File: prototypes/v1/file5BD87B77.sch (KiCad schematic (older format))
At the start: 5 parts, among them U1 74LS10, U3 74LS04, U4 74LS20, U6 74LS00, U7 74LS04

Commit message: finish logic
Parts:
- renumbered U6 to U10, U7 to U13, U3 to U2, U1 to U4, U4 to U8
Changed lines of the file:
@@
 AR Path="/5BD91A8E/5BD8F209" Ref="U?"  Part="7"
 AR Path="/5BD8F209" Ref="U?"  Part="7"
-AR Path="/5BD87B78/5BD8F209" Ref="U3"  Part="7"
-F 0 "U3" H 2180 1396 50  0000 L CNN
+AR Path="/5BD87B78/5BD8F209" Ref="U2"  Part="7"
+F 0 "U2" H 2180 1396 50  0000 L CNN
 F 1 "74LS04" H 2180 1305 50  0000 L CNN
 F 2 "" H 1950 1350 50  0001 C CNN
@@
 AR Path="/5BD91A8E/5BD8F210" Ref="U?"  Part="5"
 AR Path="/5BD8F210" Ref="U?"  Part="5"
-AR Path="/5BD87B78/5BD8F210" Ref="U6"  Part="5"
-F 0 "U6" H 2980 1396 50  0000 L CNN
+AR Path="/5BD87B78/5BD8F210" Ref="U10"  Part="5"
+F 0 "U10" H 2980 1396 50  0000 L CNN
 F 1 "74LS00" H 2980 1305 50  0000 L CNN
 F 2 "" H 2750 1350 50  0001 C CNN
@@
 AR Path="/5BD91A8E/5BD8F217" Ref="U?"  Part="7"
 AR Path="/5BD8F217" Ref="U?"  Part="7"
-AR Path="/5BD87B78/5BD8F217" Ref="U7"  Part="7"
-F 0 "U7" H 3830 1396 50  0000 L CNN
+AR Path="/5BD87B78/5BD8F217" Ref="U13"  Part="7"
+F 0 "U13" H 3830 1396 50  0000 L CNN
 F 1 "74LS04" H 3830 1305 50  0000 L CNN
 F 2 "" H 3600 1350 50  0001 C CNN
@@
 AR Path="/5BD91A8E/5BD8F224" Ref="#PWR?"  Part="1"
 AR Path="/5BD8F224" Ref="#PWR?"  Part="1"
-AR Path="/5BD87B78/5BD8F224" Ref="#PWR05"  Part="1"
-F 0 "#PWR05" H 3750 1700 50  0001 C CNN
+AR Path="/5BD87B78/5BD8F224" Ref="#PWR022"  Part="1"
+F 0 "#PWR022" H 3750 1700 50  0001 C CNN
 F 1 "GND" H 3755 1777 50  0000 C CNN
 F 2 "" H 3750 1950 50  0001 C CNN
@@
 AR Path="/5BD91A8E/5BD8F22A" Ref="#PWR?"  Part="1"
 AR Path="/5BD8F22A" Ref="#PWR?"  Part="1"
-AR Path="/5BD87B78/5BD8F22A" Ref="#PWR04"  Part="1"
-F 0 "#PWR04" H 2900 1700 50  0001 C CNN
+AR Path="/5BD87B78/5BD8F22A" Ref="#PWR021"  Part="1"
+F 0 "#PWR021" H 2900 1700 50  0001 C CNN
 F 1 "GND" H 2905 1777 50  0000 C CNN
 F 2 "" H 2900 1950 50  0001 C CNN
@@
 AR Path="/5BD91A8E/5BD8F230" Ref="#PWR?"  Part="1"
 AR Path="/5BD8F230" Ref="#PWR?"  Part="1"
-AR Path="/5BD87B78/5BD8F230" Ref="#PWR03"  Part="1"
-F 0 "#PWR03" H 2100 1700 50  0001 C CNN
+AR Path="/5BD87B78/5BD8F230" Ref="#PWR020"  Part="1"
+F 0 "#PWR020" H 2100 1700 50  0001 C CNN
 F 1 "GND" H 2105 1777 50  0000 C CNN
 F 2 "" H 2100 1950 50  0001 C CNN
@@
 AR Path="/5BD91A8E/5BD8F23C" Ref="U?"  Part="3"
 AR Path="/5BD8F23C" Ref="U?"  Part="3"
-AR Path="/5BD87B78/5BD8F23C" Ref="U4"  Part="3"
-F 0 "U4" H 1330 1446 50  0000 L CNN
+AR Path="/5BD87B78/5BD8F23C" Ref="U8"  Part="3"
+F 0 "U8" H 1330 1446 50  0000 L CNN
 F 1 "74LS20" H 1330 1355 50  0000 L CNN
 F 2 "" H 1100 1400 50  0001 C CNN
@@
 AR Path="/5BD91A8E/5BD8F244" Ref="#PWR?"  Part="1"
 AR Path="/5BD8F244" Ref="#PWR?"  Part="1"
-AR Path="/5BD87B78/5BD8F244" Ref="#PWR01"  Part="1"
-F 0 "#PWR01" H 1250 1700 50  0001 C CNN
+AR Path="/5BD87B78/5BD8F244" Ref="#PWR018"  Part="1"
+F 0 "#PWR018" H 1250 1700 50  0001 C CNN
 F 1 "GND" H 1255 1777 50  0000 C CNN
 F 2 "" H 1250 1950 50  0001 C CNN
@@
 P 4450 1350
 AR Path="/5BDA73F4" Ref="U?"  Part="4"
-AR Path="/5BD87B78/5BDA73F4" Ref="U1"  Part="4"
-F 0 "U1" H 4680 1396 50  0000 L CNN
+AR Path="/5BD87B78/5BDA73F4" Ref="U4"  Part="4"
+F 0 "U4" H 4680 1396 50  0000 L CNN
 F 1 "74LS10" H 4680 1305 50  0000 L CNN
 F 2 "" H 4450 1350 50  0001 C CNN
@@
 P 4600 1850
 AR Path="/5BDA73FC" Ref="#PWR?"  Part="1"
-AR Path="/5BD87B78/5BDA73FC" Ref="#PWR06"  Part="1"
-F 0 "#PWR06" H 4600 1600 50  0001 C CNN
+AR Path="/5BD87B78/5BDA73FC" Ref="#PWR023"  Part="1"
+F 0 "#PWR023" H 4600 1600 50  0001 C CNN
 F 1 "GND" H 4605 1677 50  0000 C CNN
 F 2 "" H 4600 1850 50  0001 C CNN
@@
 	1750 3150 1900 3150
 $Comp
-L power:+5V #PWR02
+L power:+5V #PWR019
 U 1 1 5BDEC84E
 P 1900 2950
-F 0 "#PWR02" H 1900 2800 50  0001 C CNN
+F 0 "#PWR019" H 1900 2800 50  0001 C CNN
 F 1 "+5V" H 1915 3123 50  0000 C CNN
 F 2 "" H 1900 2950 50  0001 C CNN

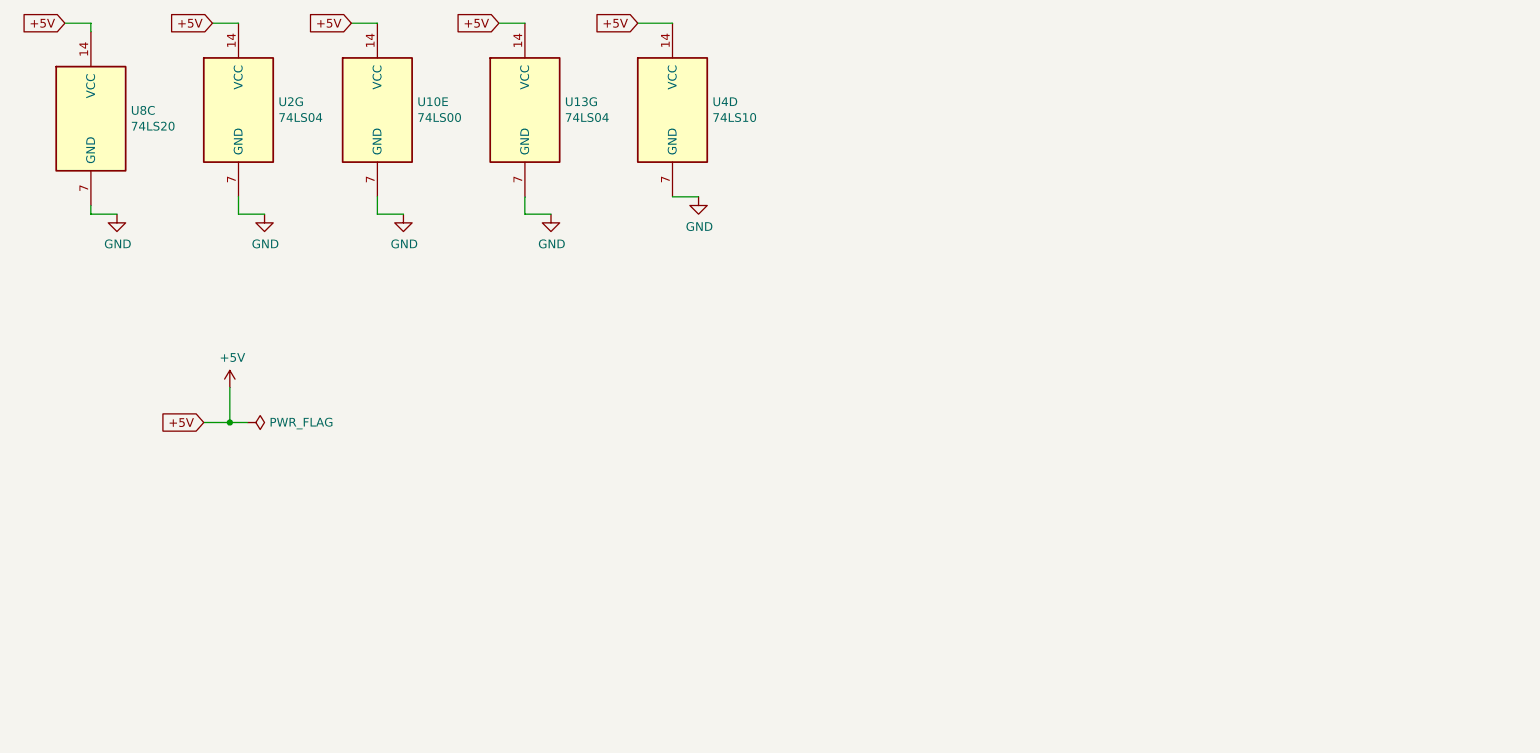
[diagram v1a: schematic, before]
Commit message: optimized logic
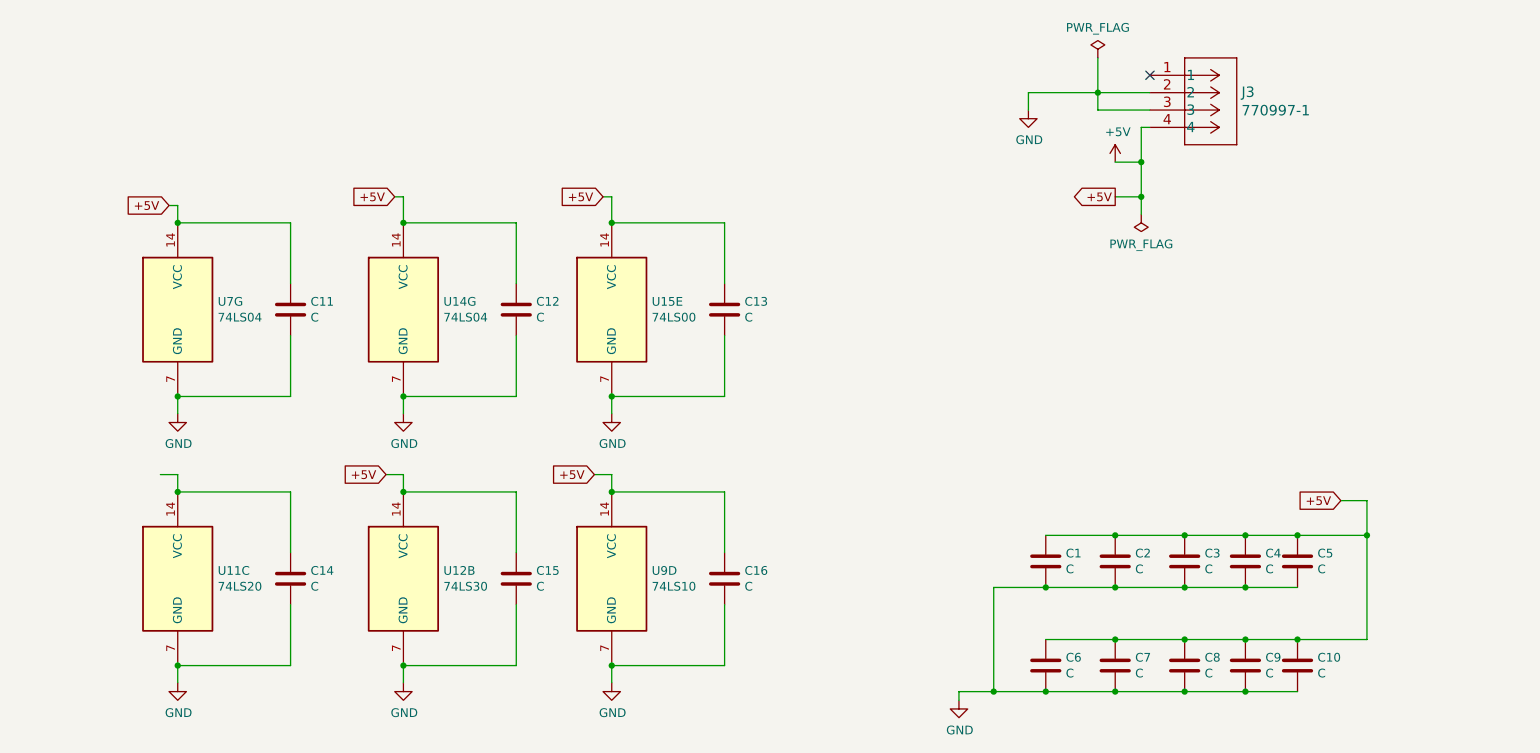
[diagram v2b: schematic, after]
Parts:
- removed U10: 74LS00, symbol 74xx:74LS00
- removed U13, U2: 74LS04, symbol 74xx:74LS04
- removed U4: 74LS10, symbol 74xx:74LS10
- removed U8: 74LS20, symbol 74xx:74LS20
- added C1: C, Capacitors_ThroughHole:C_Disc_D6.0mm_W4.4mm_P5.00mm, symbol Device:C
- added C10, C11, C12, C13, C14, C15, C16, C2, C3, C4, C5, C6, C7, C8, C9: C, symbol Device:C
- added J3: 770997-1, footprints:770997-1, symbol symbols:770997-1
- added U11: 74LS20, symbol 74xx:74LS20
- added U12: 74LS30, symbol 74xx:74LS30
- added U14, U7: 74LS04, symbol 74xx:74LS04
- added U15: 74LS00, symbol 74xx:74LS00
- added U9: 74LS10, symbol 74xx:74LS10
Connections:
- net +5V: now also C1.1, C10.1, C11.1, C12.1, C13.1, C15.1, C16.1, C2.1, C3.1, C4.1, C5.1, C6.1, C7.1, C8.1, C9.1, J3.4, U12.14 (VCC), U14.14 (VCC), U15.14 (VCC), U7.14 (VCC), U9.14 (VCC)
- net GND: now also C1.2, C10.2, C11.2, C12.2, C13.2, C14.2, C15.2, C16.2, C2.2, C3.2, C4.2, C5.2, C6.2, C7.2, C8.2, C9.2, J3.2, J3.3, U11.7 (GND), U12.7 (GND), U14.7 (GND), U15.7 (GND), U7.7 (GND), U9.7 (GND)
- new net: C14.1, U11.14 (VCC)
- no-connect marks 0 -> 1

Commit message: gerbers created, Rev 0 sent to manufacturer
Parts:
- added C17, C18, C19, C20: C, Capacitors_ThroughHole:C_Disc_D6.0mm_W4.4mm_P5.00mm, symbol Device:C
- C10, C11, C12, C13, C14, C15, C16, C2, C3, C4, C5, C6, C7, C8, C9: footprint (none) -> Capacitors_ThroughHole:C_Disc_D6.0mm_W4.4mm_P5.00mm
- U11, U12, U14, U15, U7, U9: footprint (none) -> Package_DIP:DIP-14_W7.62mm
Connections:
- net +5V: now also C14.1, U11.14 (VCC), C17.1, C18.1, C19.1, C20.1
- net GND: now also C17.2, C18.2, C19.2, C20.2
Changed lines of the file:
@@
 F 0 "C2" H 7115 3996 50  0000 L CNN
 F 1 "C" H 7115 3905 50  0000 L CNN
-F 2 "" H 7038 3800 50  0001 C CNN
+F 2 "Capacitors_ThroughHole:C_Disc_D6.0mm_W4.4mm_P5.00mm" H 7038 3800 50  0001 C CNN
 F 3 "~" H 7000 3950 50  0001 C CNN
 	1    7000 3950
@@
 F 0 "C3" H 7515 3996 50  0000 L CNN
 F 1 "C" H 7515 3905 50  0000 L CNN
-F 2 "" H 7438 3800 50  0001 C CNN
+F 2 "Capacitors_ThroughHole:C_Disc_D6.0mm_W4.4mm_P5.00mm" H 7438 3800 50  0001 C CNN
 F 3 "~" H 7400 3950 50  0001 C CNN
 	1    7400 3950
@@
 F 0 "C4" H 7865 3996 50  0000 L CNN
 F 1 "C" H 7865 3905 50  0000 L CNN
-F 2 "" H 7788 3800 50  0001 C CNN
+F 2 "Capacitors_ThroughHole:C_Disc_D6.0mm_W4.4mm_P5.00mm" H 7788 3800 50  0001 C CNN
 F 3 "~" H 7750 3950 50  0001 C CNN
 	1    7750 3950
@@
 F 0 "C5" H 8165 3996 50  0000 L CNN
 F 1 "C" H 8165 3905 50  0000 L CNN
-F 2 "" H 8088 3800 50  0001 C CNN
+F 2 "Capacitors_ThroughHole:C_Disc_D6.0mm_W4.4mm_P5.00mm" H 8088 3800 50  0001 C CNN
 F 3 "~" H 8050 3950 50  0001 C CNN
 	1    8050 3950
@@
 F 0 "C6" H 6715 4596 50  0000 L CNN
 F 1 "C" H 6715 4505 50  0000 L CNN
-F 2 "" H 6638 4400 50  0001 C CNN
+F 2 "Capacitors_ThroughHole:C_Disc_D6.0mm_W4.4mm_P5.00mm" H 6638 4400 50  0001 C CNN
 F 3 "~" H 6600 4550 50  0001 C CNN
 	1    6600 4550
@@
 F 0 "C7" H 7115 4596 50  0000 L CNN
 F 1 "C" H 7115 4505 50  0000 L CNN
-F 2 "" H 7038 4400 50  0001 C CNN
+F 2 "Capacitors_ThroughHole:C_Disc_D6.0mm_W4.4mm_P5.00mm" H 7038 4400 50  0001 C CNN
 F 3 "~" H 7000 4550 50  0001 C CNN
 	1    7000 4550
@@
 F 0 "C8" H 7515 4596 50  0000 L CNN
 F 1 "C" H 7515 4505 50  0000 L CNN
-F 2 "" H 7438 4400 50  0001 C CNN
+F 2 "Capacitors_ThroughHole:C_Disc_D6.0mm_W4.4mm_P5.00mm" H 7438 4400 50  0001 C CNN
 F 3 "~" H 7400 4550 50  0001 C CNN
 	1    7400 4550
@@
 F 0 "C9" H 7865 4596 50  0000 L CNN
 F 1 "C" H 7865 4505 50  0000 L CNN
-F 2 "" H 7788 4400 50  0001 C CNN
+F 2 "Capacitors_ThroughHole:C_Disc_D6.0mm_W4.4mm_P5.00mm" H 7788 4400 50  0001 C CNN
 F 3 "~" H 7750 4550 50  0001 C CNN
 	1    7750 4550
@@
 F 0 "C10" H 8165 4596 50  0000 L CNN
 F 1 "C" H 8165 4505 50  0000 L CNN
-F 2 "" H 8088 4400 50  0001 C CNN
+F 2 "Capacitors_ThroughHole:C_Disc_D6.0mm_W4.4mm_P5.00mm" H 8088 4400 50  0001 C CNN
 F 3 "~" H 8050 4550 50  0001 C CNN
 	1    8050 4550
@@
 Wire Wire Line
 	7750 4400 8050 4400
-Text GLabel 8300 3600 0    50   Input ~ 0
+Text GLabel 9200 3600 0    50   Input ~ 0
 +5V
 $Comp
@@
 F 0 "U7" H 1830 2546 50  0000 L CNN
 F 1 "74LS04" H 1830 2455 50  0000 L CNN
-F 2 "" H 1600 2500 50  0001 C CNN
+F 2 "Package_DIP:DIP-14_W7.62mm" H 1600 2500 50  0001 C CNN
 F 3 "http://www.ti.com/lit/gpn/sn74LS04" H 1600 2500 50  0001 C CNN
 	7    1600 2500
@@
 F 0 "U14" H 3130 2546 50  0000 L CNN
 F 1 "74LS04" H 3130 2455 50  0000 L CNN
-F 2 "" H 2900 2500 50  0001 C CNN
+F 2 "Package_DIP:DIP-14_W7.62mm" H 2900 2500 50  0001 C CNN
 F 3 "http://www.ti.com/lit/gpn/sn74LS04" H 2900 2500 50  0001 C CNN
 	7    2900 2500
@@
 F 0 "U15" H 4330 2546 50  0000 L CNN
 F 1 "74LS00" H 4330 2455 50  0000 L CNN
-F 2 "" H 4100 2500 50  0001 C CNN
+F 2 "Package_DIP:DIP-14_W7.62mm" H 4100 2500 50  0001 C CNN
 F 3 "http://www.ti.com/lit/gpn/sn74ls00" H 4100 2500 50  0001 C CNN
 	5    4100 2500
@@
 F 0 "U9" H 4330 4096 50  0000 L CNN
 F 1 "74LS10" H 4330 4005 50  0000 L CNN
-F 2 "" H 4100 4050 50  0001 C CNN
+F 2 "Package_DIP:DIP-14_W7.62mm" H 4100 4050 50  0001 C CNN
 F 3 "http://www.ti.com/lit/gpn/sn74LS10" H 4100 4050 50  0001 C CNN
 	4    4100 4050
@@
 F 0 "U11" H 1830 4096 50  0000 L CNN
 F 1 "74LS20" H 1830 4005 50  0000 L CNN
-F 2 "" H 1600 4050 50  0001 C CNN
+F 2 "Package_DIP:DIP-14_W7.62mm" H 1600 4050 50  0001 C CNN
 F 3 "http://www.ti.com/lit/gpn/sn74LS20" H 1600 4050 50  0001 C CNN
 	3    1600 4050
@@
 F 0 "U12" H 3130 4096 50  0000 L CNN
 F 1 "74LS30" H 3130 4005 50  0000 L CNN
-F 2 "" H 2900 4050 50  0001 C CNN
+F 2 "Package_DIP:DIP-14_W7.62mm" H 2900 4050 50  0001 C CNN
 F 3 "http://www.ti.com/lit/gpn/sn74LS30" H 2900 4050 50  0001 C CNN
 	2    2900 4050
@@
 F 0 "C15" H 3665 4096 50  0000 L CNN
 F 1 "C" H 3665 4005 50  0000 L CNN
-F 2 "" H 3588 3900 50  0001 C CNN
+F 2 "Capacitors_ThroughHole:C_Disc_D6.0mm_W4.4mm_P5.00mm" H 3588 3900 50  0001 C CNN
 F 3 "~" H 3550 4050 50  0001 C CNN
 	1    3550 4050
@@
 F 0 "C14" H 2365 4096 50  0000 L CNN
 F 1 "C" H 2365 4005 50  0000 L CNN
-F 2 "" H 2288 3900 50  0001 C CNN
+F 2 "Capacitors_ThroughHole:C_Disc_D6.0mm_W4.4mm_P5.00mm" H 2288 3900 50  0001 C CNN
 F 3 "~" H 2250 4050 50  0001 C CNN
 	1    2250 4050
@@
 F 0 "C16" H 4865 4096 50  0000 L CNN
 F 1 "C" H 4865 4005 50  0000 L CNN
-F 2 "" H 4788 3900 50  0001 C CNN
+F 2 "Capacitors_ThroughHole:C_Disc_D6.0mm_W4.4mm_P5.00mm" H 4788 3900 50  0001 C CNN
 F 3 "~" H 4750 4050 50  0001 C CNN
 	1    4750 4050
@@
 F 0 "C11" H 2365 2546 50  0000 L CNN
 F 1 "C" H 2365 2455 50  0000 L CNN
-F 2 "" H 2288 2350 50  0001 C CNN
+F 2 "Capacitors_ThroughHole:C_Disc_D6.0mm_W4.4mm_P5.00mm" H 2288 2350 50  0001 C CNN
 F 3 "~" H 2250 2500 50  0001 C CNN
 	1    2250 2500
@@
 F 0 "C12" H 3665 2546 50  0000 L CNN
 F 1 "C" H 3665 2455 50  0000 L CNN
-F 2 "" H 3588 2350 50  0001 C CNN
+F 2 "Capacitors_ThroughHole:C_Disc_D6.0mm_W4.4mm_P5.00mm" H 3588 2350 50  0001 C CNN
 F 3 "~" H 3550 2500 50  0001 C CNN
 	1    3550 2500
@@
 F 0 "C13" H 4865 2546 50  0000 L CNN
 F 1 "C" H 4865 2455 50  0000 L CNN
-F 2 "" H 4788 2350 50  0001 C CNN
+F 2 "Capacitors_ThroughHole:C_Disc_D6.0mm_W4.4mm_P5.00mm" H 4788 2350 50  0001 C CNN
 F 3 "~" H 4750 2500 50  0001 C CNN
 	1    4750 2500
@@
 Connection ~ 1600 3000
 Wire Wire Line
-	8050 3800 8450 3800
-Wire Wire Line
-	8450 3800 8450 4400
-Wire Wire Line
-	8450 4400 8050 4400
+	9350 3800 9350 4400
+Wire Wire Line
+	9200 3600 9350 3600
+Wire Wire Line
+	9350 3600 9350 3800
+Connection ~ 9350 3800
+$Comp
+L Device:C C17
+U 1 1 5BDD839C
+P 8350 3950
+F 0 "C17" H 8465 3996 50  0000 L CNN
+F 1 "C" H 8465 3905 50  0000 L CNN
+F 2 "Capacitors_ThroughHole:C_Disc_D6.0mm_W4.4mm_P5.00mm" H 8388 3800 50  0001 C CNN
+F 3 "~" H 8350 3950 50  0001 C CNN
+	1    8350 3950
+	1    0    0    -1
+$EndComp
+$Comp
+L Device:C C19
+U 1 1 5BDD83FC
+P 8650 3950
+F 0 "C19" H 8765 3996 50  0000 L CNN
+F 1 "C" H 8765 3905 50  0000 L CNN
+F 2 "Capacitors_ThroughHole:C_Disc_D6.0mm_W4.4mm_P5.00mm" H 8688 3800 50  0001 C CNN
+F 3 "~" H 8650 3950 50  0001 C CNN
+	1    8650 3950
+	1    0    0    -1
+$EndComp
+$Comp
+L Device:C C18
+U 1 1 5BDD844C
+P 8350 4550
+F 0 "C18" H 8465 4596 50  0000 L CNN
+F 1 "C" H 8465 4505 50  0000 L CNN
+F 2 "Capacitors_ThroughHole:C_Disc_D6.0mm_W4.4mm_P5.00mm" H 8388 4400 50  0001 C CNN
+F 3 "~" H 8350 4550 50  0001 C CNN
+	1    8350 4550
+	1    0    0    -1
+$EndComp
+$Comp
+L Device:C C20
+U 1 1 5BDD84AE
+P 8650 4550
+F 0 "C20" H 8765 4596 50  0000 L CNN
+F 1 "C" H 8765 4505 50  0000 L CNN
+F 2 "Capacitors_ThroughHole:C_Disc_D6.0mm_W4.4mm_P5.00mm" H 8688 4400 50  0001 C CNN
+F 3 "~" H 8650 4550 50  0001 C CNN
+	1    8650 4550
+	1    0    0    -1
+$EndComp
+Wire Wire Line
+	8050 3800 8350 3800
 Connection ~ 8050 3800
+Connection ~ 8350 3800
+Wire Wire Line
+	8350 3800 8650 3800
+Connection ~ 8650 3800
+Wire Wire Line
+	8650 3800 9350 3800
+Wire Wire Line
+	8050 4400 8350 4400
 Connection ~ 8050 4400
-Wire Wire Line
-	8300 3600 8450 3600
-Wire Wire Line
-	8450 3600 8450 3800
-Connection ~ 8450 3800
+Connection ~ 8350 4400
+Wire Wire Line
+	8350 4400 8650 4400
+Connection ~ 8650 4400
+Wire Wire Line
+	8650 4400 9350 4400
+Wire Wire Line
+	8050 4100 8350 4100
+Connection ~ 8050 4100
+Connection ~ 8350 4100
+Wire Wire Line
+	8350 4100 8650 4100
+Wire Wire Line
+	8050 4700 8350 4700
+Connection ~ 8050 4700
+Connection ~ 8350 4700
+Wire Wire Line
+	8350 4700 8650 4700
+Text GLabel 1500 3450 0    50   Input ~ 0
++5V
 $EndSCHEMATC
